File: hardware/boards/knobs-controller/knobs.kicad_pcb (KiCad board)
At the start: 2 copper layers, 110.5 x 111.2 mm, 183 parts, among them J1 ZX62-AB-5PA(31), J10 Conn_01x01_Female, J101 WURTH_ELECTRONICS_61400413321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, J102 USB-A-S-X-X-VT, J103 ST7735_1.4, J11 Conn_01x01_Female, J12 Conn_01x01_Female, J13 Conn_01x01_Female, J14 Conn_01x01_Female, J15 Conn_01x01_Female, J16 Conn_01x01_Female, J17 Conn_01x01_Female, J18 Conn_01x01_Female, J19 Conn_01x01_Female, J2 Conn_01x01_Female, J20 Conn_01x01_Female, J21 Conn_01x01_Female, J22 Conn_01x01_Female, J23 Conn_01x01_Female, J24 Conn_01x01_Female, J25 Conn_01x01_Female, J26 Conn_01x01_Female, J27 Conn_01x01_Female, J28 Conn_01x01_Female, J29 Conn_01x01_Female, J3 Conn_01x01_Female, J30 Conn_01x01_Female, J31 Conn_01x01_Female, J32 Conn_01x01_Female, J33 Conn_01x01_Female, J34 Conn_01x01_Female, J35 Conn_01x01_Female, J36 Conn_01x01_Female, J37 Conn_01x01_Female, J38 Conn_01x01_Female, J39 Conn_01x01_Female, J4 Conn_01x01_Female, J40 Conn_01x01_Female, J41 Conn_01x01_Female, J42 Conn_01x01_Female, J43 Conn_01x01_Female, J44 Conn_01x01_Female, J45 Conn_01x01_Female, J46 Conn_01x01_Female, J47 Conn_01x01_Female, J48 Conn_01x01_Female, J49 Conn_01x01_Female, J5 Conn_01x01_Female, J50 Conn_01x01_Female, J51 Conn_01x01_Female, J52 Conn_01x01_Female, J53 Conn_01x01_Female, J54 Conn_01x01_Female, J55 Conn_01x01_Female, J56 Conn_01x01_Female, J6 Conn_01x01_Female, J7 Conn_01x01_Female, J8 2X3_SMD_MALE, J9 Conn_01x01_Female, SW1 Rotary Encoder, SW2 Rotary Encoder, SW3 Rotary Encoder, U100 ANALOG_DEVICES_AD7606BSTZANAL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, U101 ANALOG_DEVICES_AD5754BREZANAL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, U102 MICROCHIP_MCP1700T-2502E-TTMI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, U2 AP7215-33YG-13, U3 ATSAMD21G18A-48, Y1 32.768KHz

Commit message: knobsv1.7 routed
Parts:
- removed TP101, TP102, TP103, TP104, TP105, TP106, TP107, TP108, TP109: TEST-POINT3X5, topbreakout:PAD.03X.05
- moved D2 35.3 mm to (138.4, 101.6), turned to 180 degrees
- moved R30 35.2 mm to (131.4, 128.9)
- moved C12 27.6 mm to (136.5, 128.9), turned to -90 degrees
- moved C3 24.8 mm to (140.3, 128.9), turned to -90 degrees
- moved R8 23.4 mm to (131.8, 124.5)
- moved R9 19.7 mm to (124.2, 120.4)
- moved R31 19.6 mm to (146.1, 114.3)
- moved R22 18.6 mm to (159.4, 116.8)
- moved R18 14.8 mm to (134.0, 102.9)
- moved R28 14.5 mm to (176.5, 93.3), turned to -90 degrees
- moved C14 13.6 mm to (135.9, 103.5)
- moved R10 12.8 mm to (130.2, 97.8)
- moved J11 12.7 mm to (186.7, 48.3)
- moved J47 12.7 mm to (186.7, 61.0)
- moved R11 12.2 mm to (165.1, 127.6)
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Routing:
- net +3V3: track 0.00 -> 542.6 mm, vias 0 -> 7
- net VIN: track 0.00 -> 190.0 mm, vias 0 -> 4
- net AD_AGND: track 93.6 -> 240.6 mm
- net /knobs_1/PA12_S2_MOSI: track 0.00 -> 110.4 mm, vias 0 -> 2
- net SPI0_SCK: track 0.00 -> 85.1 mm, vias 0 -> 1
- net SPI0_MOSI: track 0.00 -> 84.5 mm
- net /knobs_1/PB22_S5_TX: track 0.00 -> 79.4 mm, vias 0 -> 2
- net /knobs_1/PA04_AIN4: track 0.00 -> 78.5 mm
- net /knobs_1/PB23_S5_RX: track 0.00 -> 76.1 mm, vias 0 -> 2
- net AVDD: track 0.00 -> 68.5 mm, vias 0 -> 1
- net /knobs_1/PB11_TCC0-W5: track 0.00 -> 65.2 mm, vias 0 -> 1
- net AD_CONVST: track 0.00 -> 61.5 mm
- net AD_V8: track 0.00 -> 60.4 mm, vias 0 -> 1
- net Net-(R24-Pad1): track 0.00 -> 57.9 mm, vias 0 -> 3
- net MIDI_OUT_PIN5: track 0.00 -> 57.6 mm
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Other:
- board text removed: "AD_CONVST"

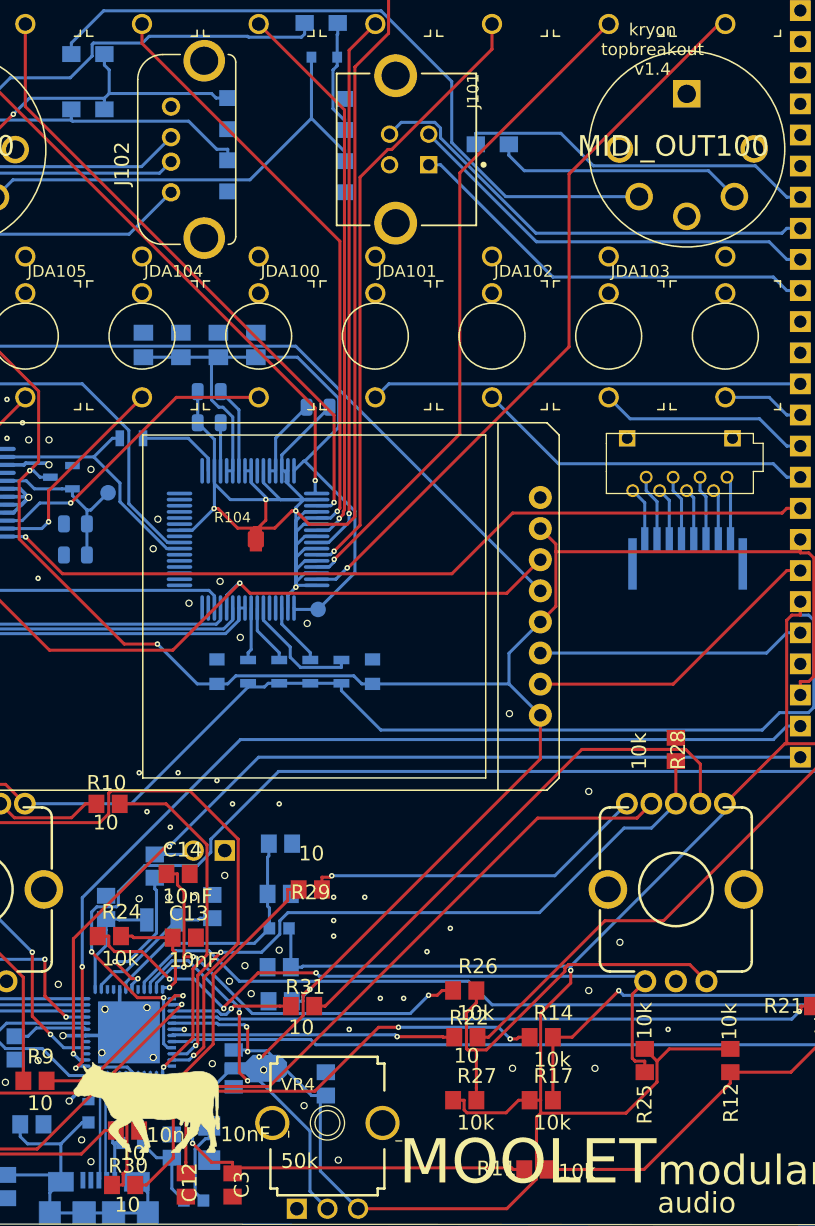
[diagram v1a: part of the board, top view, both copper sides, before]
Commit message: breakout v1.7: corrections after DRC check
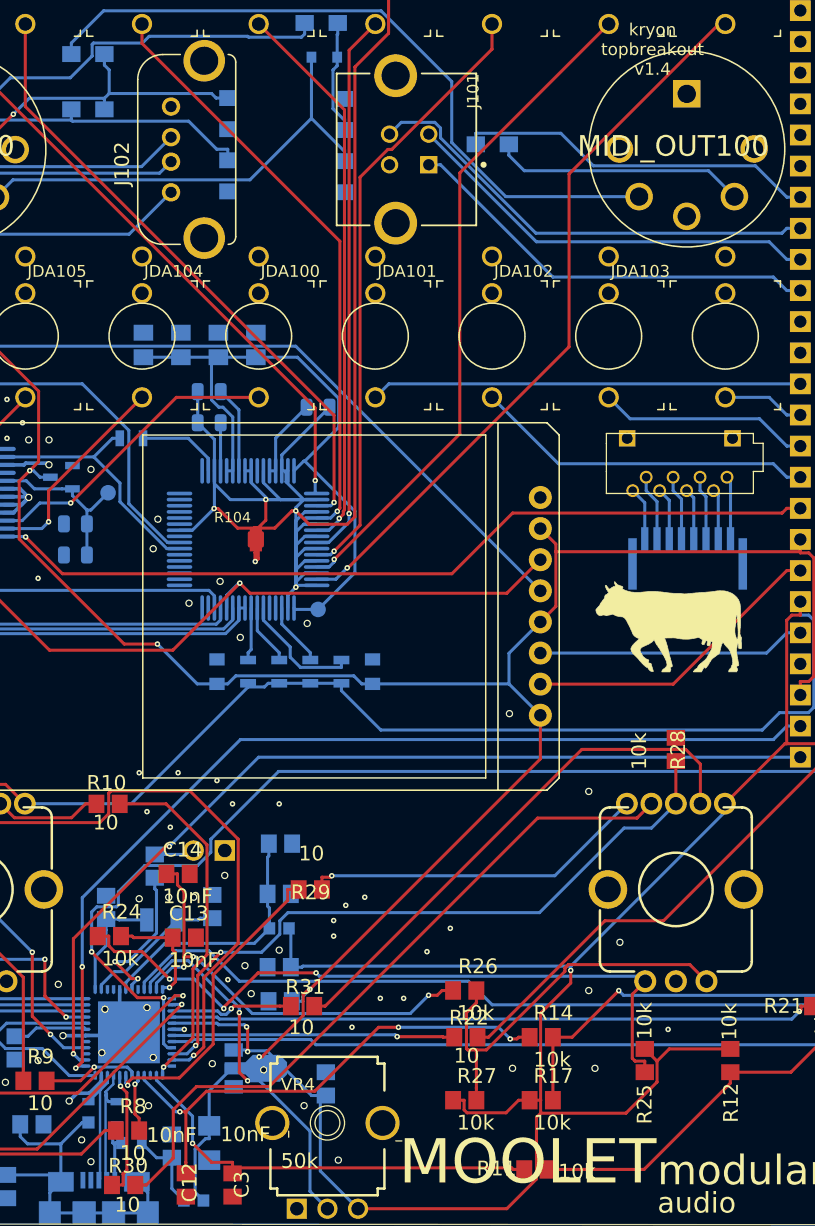
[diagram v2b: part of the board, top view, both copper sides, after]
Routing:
- net GND: track 32.5 -> 34.4 mm, vias 81 -> 82

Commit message: breakout tidyup
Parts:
- U$102: value OPTO_DARL_6N138S -> 6N138S
- moved C14 1.27 mm to (136.3, 104.7)
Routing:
- net /knobs_1/PA06_AIN6: track 36.7 -> 35.3 mm
- net GND: vias 82 -> 83
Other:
- board size 110.5 x 111.2 mm -> 110.5 x 111.1 mm
- board text added: "01/01/2020"
- board text added: "AD_BUSY"
- board text added: "AD_CONVST"
- board text added: "AVSS"
- board text added: "USB_A_D+"
- board text added: "USB_A_D-"
- board text added: "USB_A_VCC"
- board text added: "breakout board"
- board text added: "instruments"
- board text added: "v1.7"
- board text removed: "22/12/2019"
- board text removed: "AD_VREF"
- board text removed: "MOOLET instruments"
- board text removed: "Top breakout board"
- board text removed: "VIN (5v)"

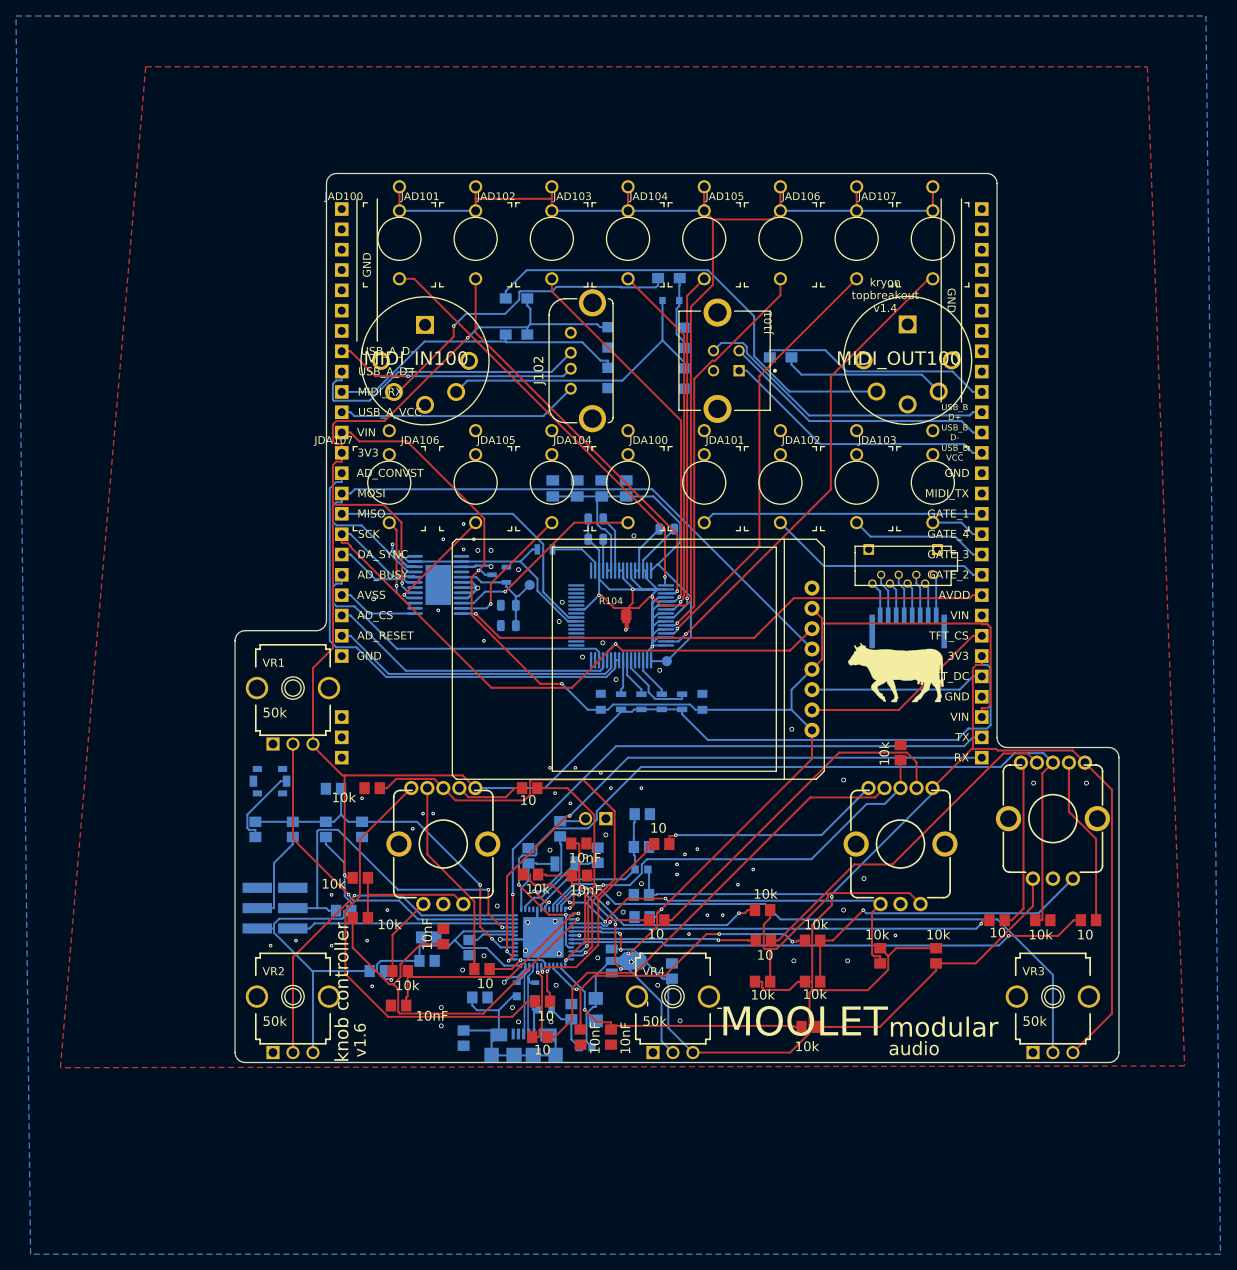
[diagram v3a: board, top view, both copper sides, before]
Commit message: correction: removed AVIN replaced with VIN
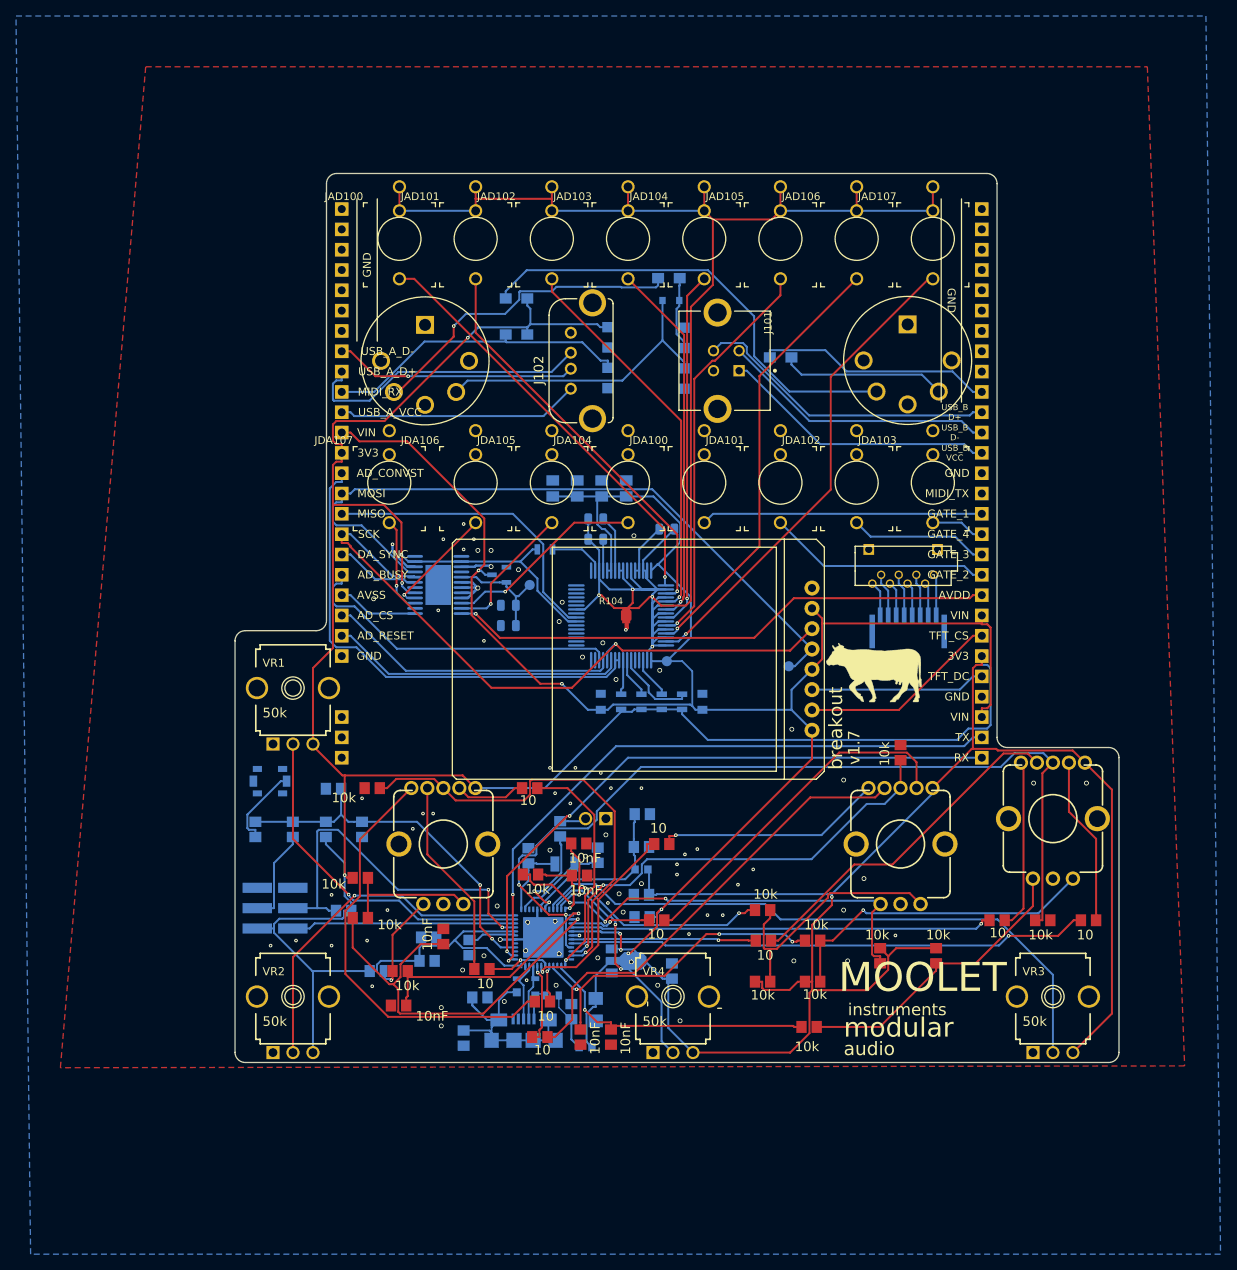
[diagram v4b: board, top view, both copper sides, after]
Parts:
- added TP108: TEST-POINT3X5, topbreakout:PAD.03X.05, B.Cu at (162.6, 82.5)
- U$102: value 6N138S -> OPTO_DARL_6N138S
- moved F2 1.99 mm to (133.0, 123.7)
- moved J1 1.87 mm to (129.4, 129.7)
- moved D1 0.49 mm to (129.7, 122.6)
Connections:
- C100 pad 1: /AD7606/AVIN -> VIN
- C101 pad 1: /AD7606/AVIN -> VIN
- C102 pad 1: /AD7606/AVIN -> VIN
- C103 pad 1: /AD7606/AVIN -> VIN
- TP100 pad P$1: /AD7606/AVIN -> VIN
- U100 pad 1: /AD7606/AVIN -> VIN
- U100 pad 37: /AD7606/AVIN -> VIN
- U100 pad 38: /AD7606/AVIN -> VIN
- U100 pad 42: /AD7606/AD_REFINOUT -> (no net)
- U100 pad 48: /AD7606/AVIN -> VIN
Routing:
- net VIN: track 190.0 -> 250.6 mm
- net /AD7606/AVIN: track 52.6 -> 0.00 mm
- net SPI0_MOSI: track 84.5 -> 88.3 mm
- net /knobs_1/USB_P: track 11.6 -> 7.97 mm
- net GND: track 34.4 -> 31.1 mm, vias 83 -> 81
- net /knobs_1/USB_N: track 10.4 -> 8.65 mm
- net Net-(C6-Pad1): track 29.1 -> 30.4 mm
- net Net-(D1-Pad4): track 5.76 -> 4.53 mm
- net Net-(C4-Pad1): track 6.85 -> 7.59 mm
- net /knobs_1/PA06_AIN6: track 35.3 -> 34.8 mm
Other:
- board text added: "breakout"
- board text removed: "knob controller"
- board text removed: "kryon topbreakout v1.4"
- board text removed: "v1.6"

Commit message: mainboard v1.7
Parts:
- removed the J27 at (106.7, 66.0)
- removed JDA107: THONKICONNNEW, topbreakout:WQP-PJ301M-12_JACK
- removed MIDI_OUT100: OG-MIDI_MAB5SHCUI-SD-50BV, topbreakout:OG-MIDI_SD-50BV
- added J50: Conn_01x01_Female, Connector_PinSocket_2.54mm:PinSocket_1x01_P2.54mm_Vertical, B.Cu at (106.7, 66.0)
- added JDA8: THONKICONNNEW, topbreakout:WQP-PJ301M-12_JACK, F.Cu at (113.9, 59.6)
- added MIDI_OUT1: OG-MIDI_MAB5SHCUI-SD-50BV, topbreakout:OG-MIDI_SD-50BV, F.Cu at (177.4, 44.3)
- renumbered C6 to C1, C2 to C10, C13 to C11, C14 to C12, C19 to C13, C32 to C14, C28 to C15, C29 to C16, C30 to C17, C27 to C18, C8 to C19, C4 to C2, C10 to C20, C100 to C21, C101 to C22, C102 to C23, C103 to C24, C104 to C25, C105 to C26, C106 to C27, C107 to C28, C108 to C29, C7 to C3, C109 to C30, C110 to C31, C11 to C4, C9 to C5, C5 to C6, C3 to C7, C12 to C8, C1 to C9, D100 to D3, F2 to F1, J40 to J10, J41 to J11, J42 to J12, J43 to J13, J44 to J14, J45 to J15, J46 to J16, J47 to J17, J48 to J18, J49 to J19, J8 to J2, J50 to J20, J51 to J21, J52 to J22, J53 to J23, J54 to J24, J55 to J25, J56 to J26, J2 to J27, J3 to J28, J5 to J29, J4 to J3, J6 to J30, J7 to J31, J9 to J32, J10 to J33, J11 to J34, J12 to J35, J13 to J36, J14 to J37, J15 to J38, J16 to J39, J34 to J4, J17 to J40, J18 to J41, J19 to J42, J20 to J43, J21 to J44, J22 to J45, J23 to J46, J24 to J47, J25 to J48, J26 to J49, J35 to J5, J28 to J51, J29 to J52, J30 to J53, J31 to J54, J32 to J55, J33 to J56, J101 to J57, J102 to J58, J103 to J59, J36 to J6, J37 to J7, J38 to J8, J39 to J9, JAD100 to JAD1, JAD101 to JAD2, JAD102 to JAD3, JAD103 to JAD4, JAD104 to JAD5, JAD105 to JAD6, JAD106 to JAD7, JAD107 to JAD8, JDA100 to JDA1, JDA101 to JDA2, JDA102 to JDA3, JDA103 to JDA4, JDA104 to JDA5, JDA105 to JDA6, JDA106 to JDA7, L2 to L1, L6 to L2, MIDI_IN100 to MIDI_IN1, R2 to R1, R14 to R10, R17 to R11, R19 to R12, R21 to R13, R22 to R14, R23 to R15, R1 to R16, R3 to R17, R4 to R18, R5 to R19, R15 to R2, R6 to R20, R8 to R21, R9 to R22, R10 to R23, R13 to R3, R100 to R32, R101 to R33, R102 to R34, R103 to R35, R104 to R36, R105 to R37, R106 to R38, R107 to R39, R7 to R4, R108 to R40, R109 to R41, R16 to R5, R20 to R6, R18 to R7, R11 to R8, R12 to R9, SW2 to SW1, SW1 to SW2, TP100 to TP1, TP108 to TP2, TP110 to TP3, U$9 to U$1, U$100 to U$2, U$101 to U$3, U$102 to U$4, U3 to U1, U100 to U3, U101 to U4, U102 to U5
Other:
- board text removed: "AVIN"

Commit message: knobs v1.7 finalisation
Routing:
- net +3V3: track 542.6 -> 544.0 mm
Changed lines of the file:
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@@
     (thickness 1.6)
     (drawings 316)
-    (tracks 1356)
+    (tracks 1360)
     (zones 0)
     (modules 175)
@@
   (segment (start 121.8012 96.1962) (end 123.38 97.775) (width 0.25) (layer Top) (net 45))
   (segment (start 107.0478 96.1962) (end 121.8012 96.1962) (width 0.25) (layer Top) (net 45))
-  (segment (start 114.1446 64.5767) (end 114.1446 68.6183) (width 0.25) (layer Top) (net 45))
-  (segment (start 111.9446 62.3767) (end 114.1446 64.5767) (width 0.25) (layer Top) (net 45))
   (segment (start 105.5797 62.3767) (end 111.9446 62.3767) (width 0.25) (layer Top) (net 45))
   (segment (start 105.5797 57.3929) (end 105.5797 62.3767) (width 0.25) (layer Top) (net 45))
@@
   (segment (start 165.4903 123.0417) (end 172.4525 123.0417) (width 0.25) (layer Top) (net 45))
   (segment (start 174.9904 118.7954) (end 173.99 117.795) (width 0.25) (layer Top) (net 45))
+  (segment (start 114.384002 63.5) (end 113.03 63.5) (width 0.25) (layer Top) (net 45))
+  (segment (start 114.969001 64.084999) (end 114.384002 63.5) (width 0.25) (layer Top) (net 45))
+  (segment (start 114.969001 66.640999) (end 114.969001 64.084999) (width 0.25) (layer Top) (net 45))
+  (segment (start 114.1446 67.4654) (end 114.969001 66.640999) (width 0.25) (layer Top) (net 45))
+  (segment (start 111.9446 62.3767) (end 113.03 63.5) (width 0.25) (layer Top) (net 45))
+  (segment (start 114.1446 67.4654) (end 114.1446 68.6183) (width 0.25) (layer Top) (net 45))
   (via (at 127.3435 118.1913) (size 0.45) (layers Top Bottom) (net 46))
   (via (at 135.1722 101.2693) (size 0.45) (layers Top Bottom) (net 46))
@@
   (segment (start 114.4945 73.6269) (end 123.419 64.7024) (width 0.25) (layer Top) (net 88))
   (via (at 113.5352 72.4934) (size 0.45) (layers Top Bottom) (net 89))
-  (segment (start 113.5352 65.5122) (end 112.624 64.601) (width 0.25) (layer Top) (net 89))
-  (segment (start 113.5352 72.4934) (end 113.5352 65.5122) (width 0.25) (layer Top) (net 89))
   (segment (start 114.8605 74.665) (end 115.845 74.665) (width 0.25) (layer Bottom) (net 89))
   (segment (start 113.5353 73.3398) (end 114.8605 74.665) (width 0.25) (layer Bottom) (net 89))
   (segment (start 113.5353 72.4934) (end 113.5353 73.3398) (width 0.25) (layer Bottom) (net 89))
   (segment (start 113.5352 72.4934) (end 113.5353 72.4934) (width 0.25) (layer Bottom) (net 89))
+  (segment (start 113.5352 64.9598) (end 113.766278 64.728722) (width 0.25) (layer Top) (net 89))
+  (segment (start 113.5352 72.4934) (end 113.5352 64.9598) (width 0.25) (layer Top) (net 89))
   (via (at 120.6798 40.0285) (size 0.45) (layers Top Bottom) (net 90))
   (segment (start 122.1951 38.5132) (end 120.6798 40.0285) (width 0.25) (layer Bottom) (net 90))

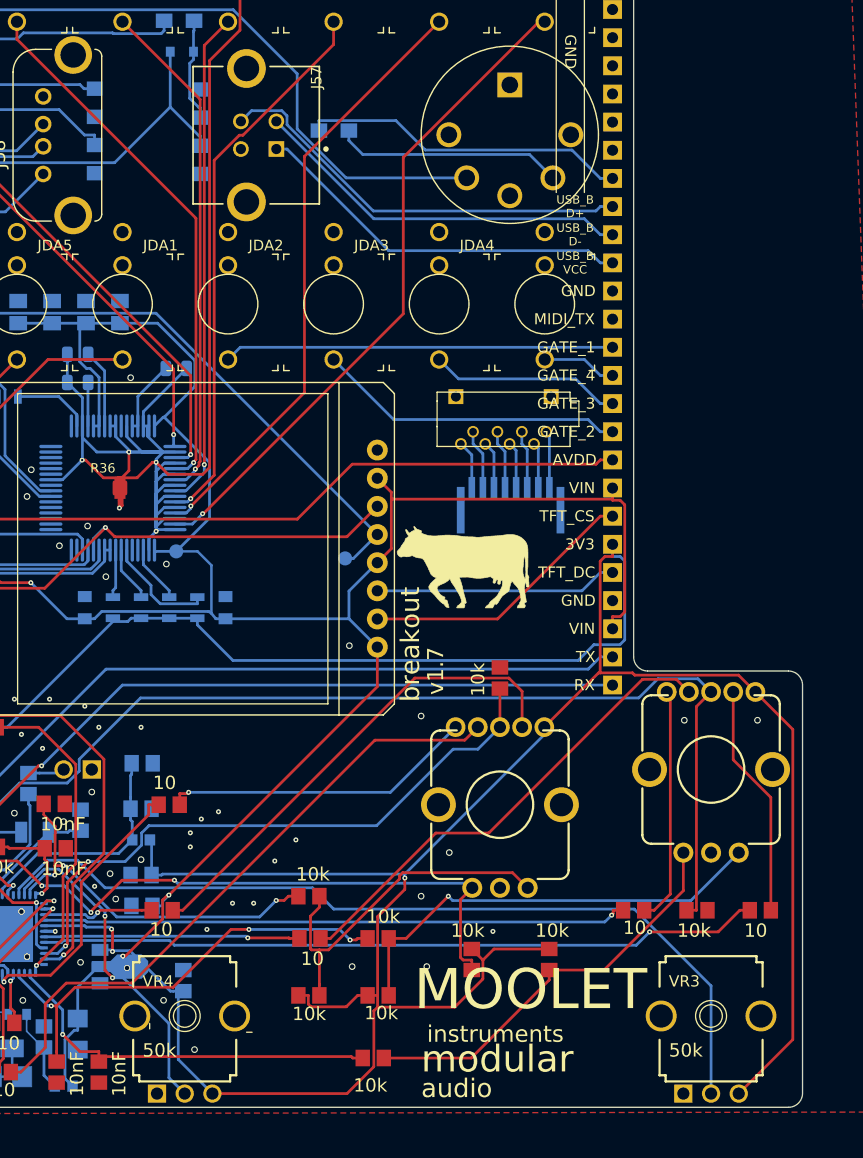
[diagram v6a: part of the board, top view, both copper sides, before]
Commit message: corrections to pcb,v1.7b
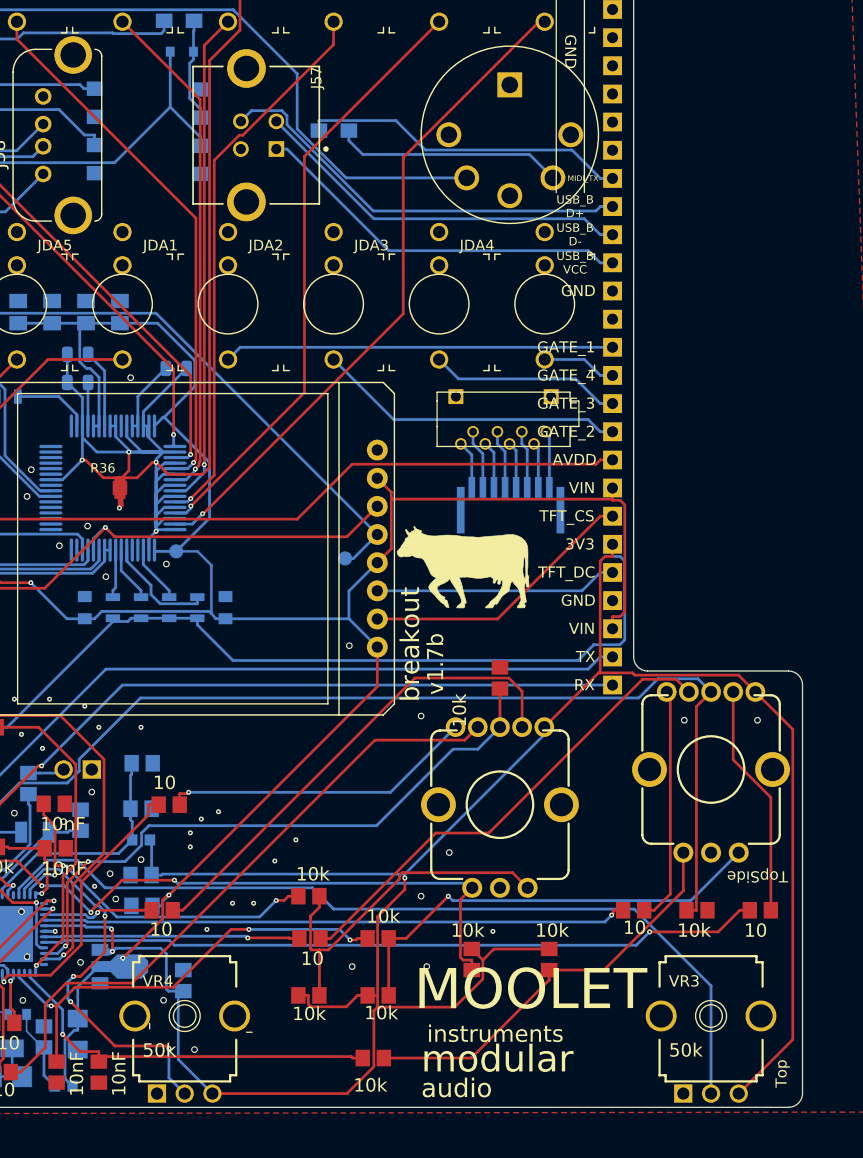
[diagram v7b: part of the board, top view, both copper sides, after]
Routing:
- net /knobs_1/PA05_AIN5: track 30.1 -> 35.4 mm, vias 2 -> 4
- net +3V3: track 544.0 -> 546.9 mm
- net (no net): vias 1 -> 0
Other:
- board text added: "26/01/2020"
- board text added: "Bottom"
- board text added: "Top"
- board text added: "TopSide"
- board text added: "v1.7b"
- board text removed: "01/01/2020"
- board text removed: "v1.7"
